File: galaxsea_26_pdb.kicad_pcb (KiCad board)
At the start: 2 copper layers, 81.5 x 54.1 mm, 18 parts, among them J1 Conn_01x10_Pin, J2 Conn_01x10_Pin, J4 Conn_01x10_Pin, U1 TPS54531DDA

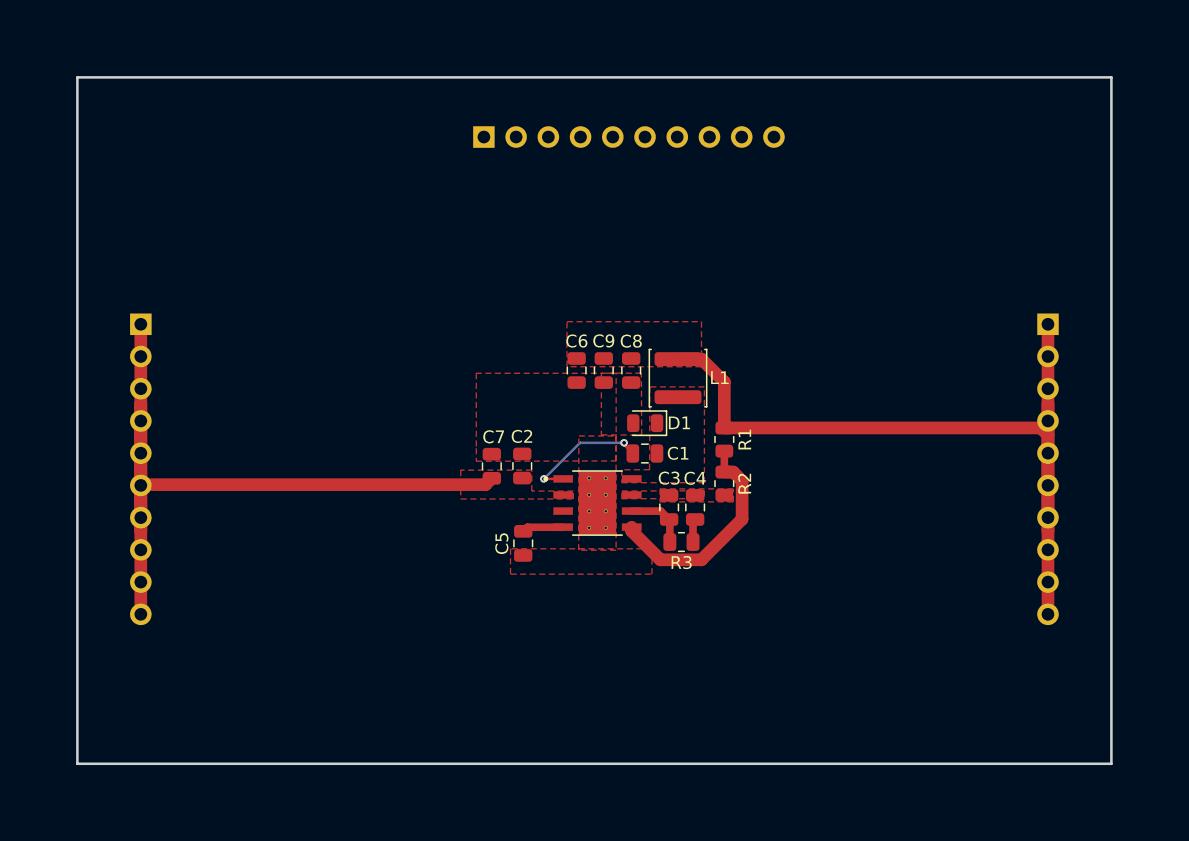
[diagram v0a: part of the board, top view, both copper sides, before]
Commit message: Add dimensions
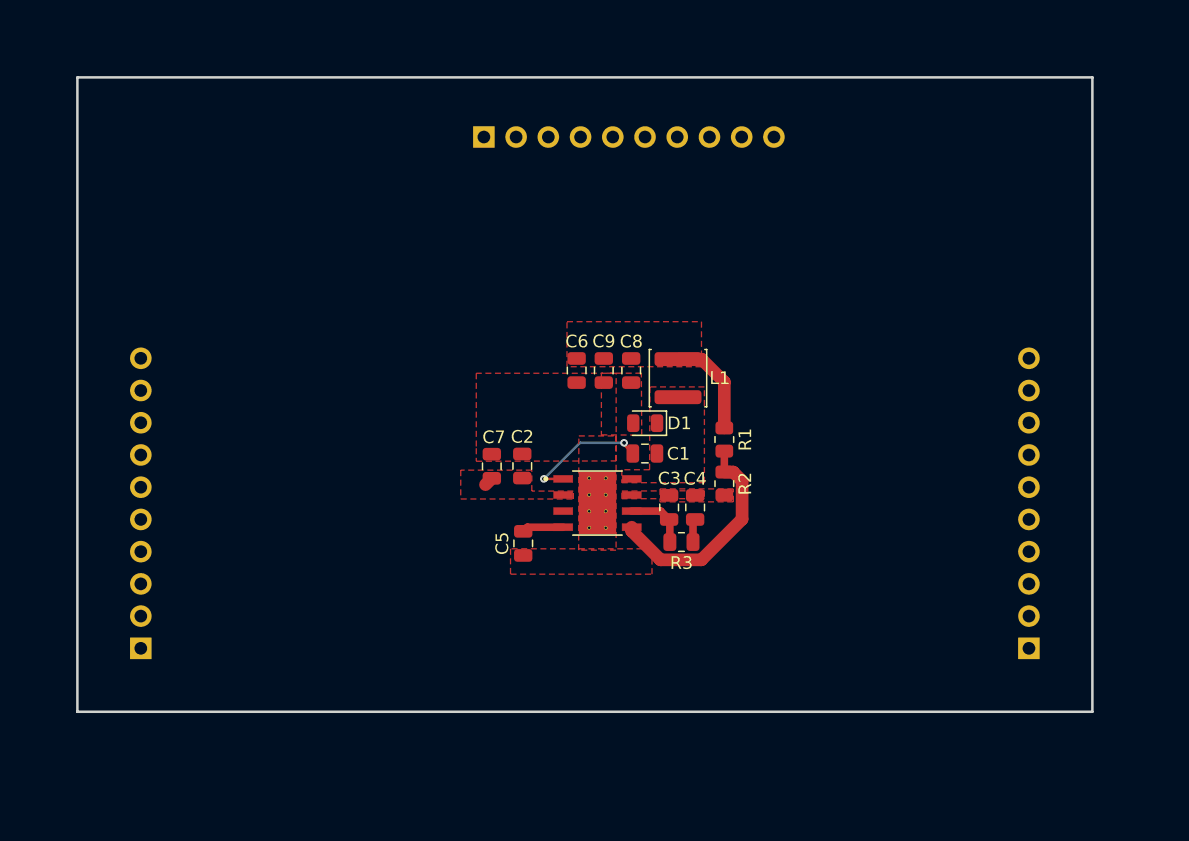
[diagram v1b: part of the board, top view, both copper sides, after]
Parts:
- moved J1 25.6 mm to (185.0, 102.8), turned to 0 degrees
- moved J2 25.5 mm to (115.0, 102.8), turned to 0 degrees
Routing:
- net /BDC_VIN: track 61.0 -> 0.74 mm
- net /BDC_VOUT: track 66.8 -> 8.02 mm
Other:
- board size 81.5 x 54.1 mm -> 80 x 50 mm

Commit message: Final pin placement
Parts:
- moved J4 27.0 mm to (115.0, 62.8)
- moved C4 0.43 mm to (158.3, 91.9)
- moved L1 0.43 mm to (156.9, 81.7)
- moved R2 0.43 mm to (160.6, 90.0)
- moved R3 0.43 mm to (157.2, 94.6)
- moved U1 0.43 mm to (150.6, 91.5)
- moved C2 0.43 mm to (144.7, 88.6)
- moved C8 0.43 mm to (153.3, 81.1)
- moved C9 0.43 mm to (151.1, 81.1)
- moved D1 0.43 mm to (154.4, 85.2)
- moved R1 0.43 mm to (160.6, 86.5)
- moved C1 0.43 mm to (154.3, 87.6)
- moved C3 0.43 mm to (156.2, 91.9)
- moved C5 0.43 mm to (144.7, 94.7)
- moved C6 0.43 mm to (149.0, 81.1)
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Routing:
- net /BDC_VIN: track 0.74 -> 51.1 mm
- net /BDC_VOUT: track 8.02 -> 55.5 mm
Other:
- board text added: "Pin 1 of each header is 5mm from corner"

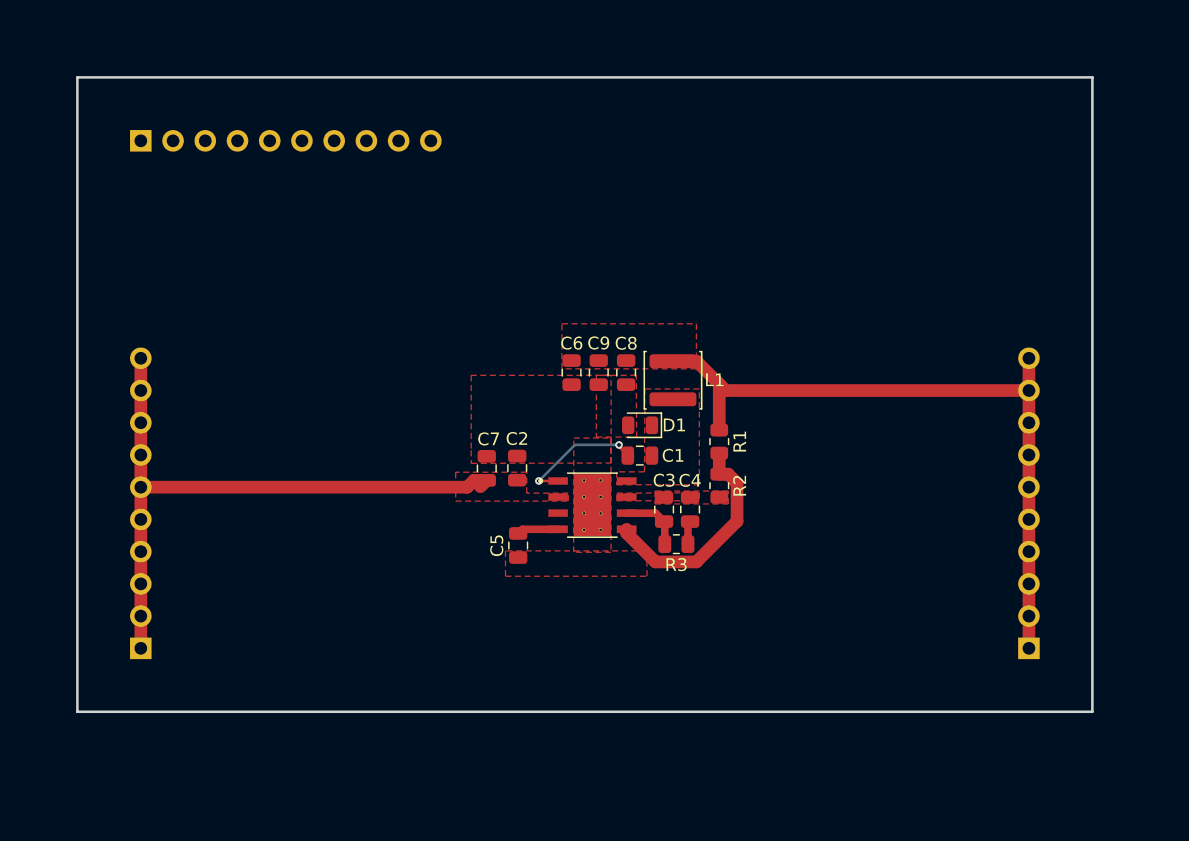
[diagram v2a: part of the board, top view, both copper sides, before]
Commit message: Organize, make BDC Module more solderable
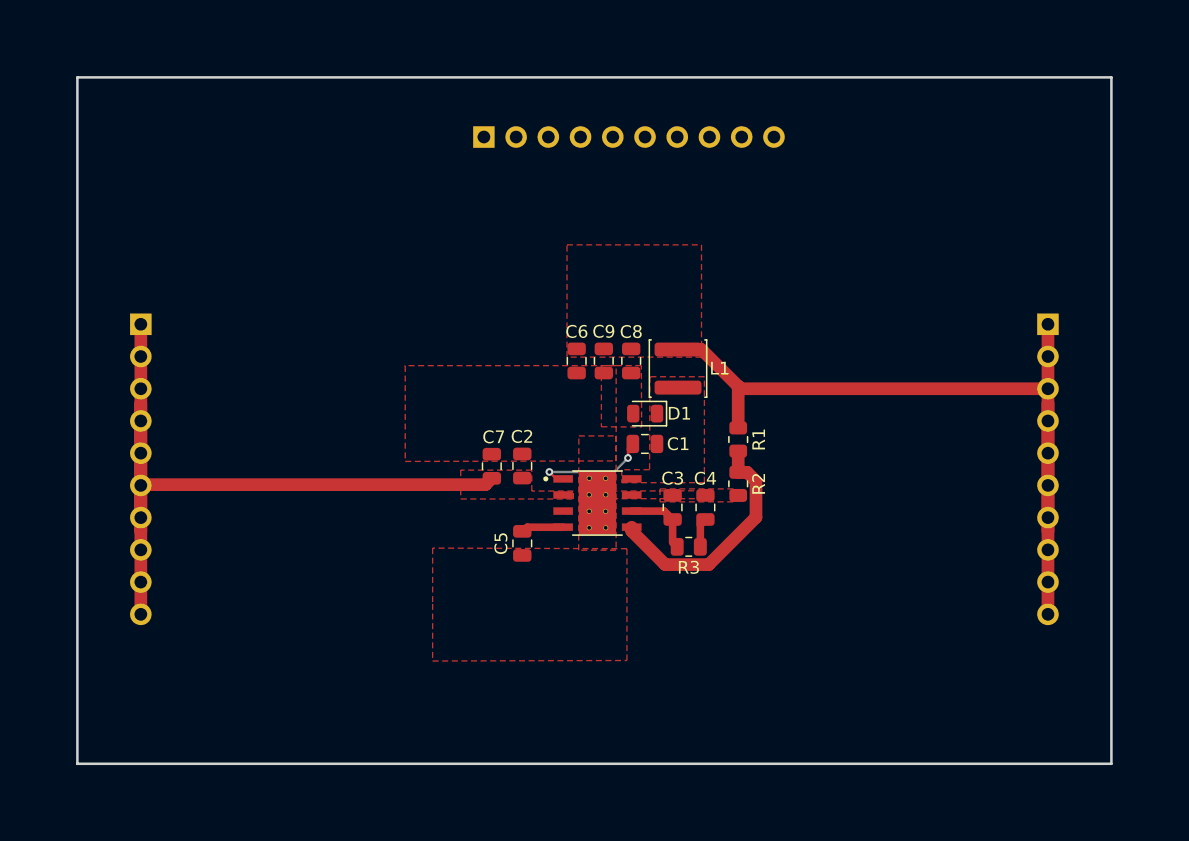
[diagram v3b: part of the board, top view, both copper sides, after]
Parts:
- moved J4 27.0 mm to (142.0, 62.5)
- moved J1 25.6 mm to (186.5, 77.3), turned to 180 degrees
- moved J2 25.5 mm to (115.0, 77.3), turned to 180 degrees
- moved R1 1.50 mm to (162.1, 86.3)
- moved R2 1.50 mm to (162.1, 89.8)
- moved C4 1.22 mm to (159.5, 91.7)
- moved D1 1.00 mm to (154.8, 84.3)
- moved L1 1.00 mm to (157.3, 80.8)
- moved C1 1.00 mm to (154.7, 86.7)
- moved C8 1.00 mm to (153.7, 80.2)
- moved C9 1.00 mm to (151.5, 80.2)
- moved C6 1.00 mm to (149.3, 80.2)
- moved R3 1.00 mm to (158.2, 94.8)
- moved C3 0.69 mm to (156.9, 91.7)
- moved U1 0.43 mm to (151.0, 91.3)
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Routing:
- net /BDC_VOUT: track 55.5 -> 66.7 mm
- net /BDC_VIN: track 51.1 -> 60.8 mm
- net /_BDC_VSENSE: track 17.6 -> 18.9 mm
- net /_BDC_BOOT: track 10.1 -> 9.24 mm
- net /_BDC_COMP: track 5.03 -> 5.80 mm
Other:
- board size 80 x 50 mm -> 81.5 x 54.1 mm
- board text removed: "Pin 1 of each header is 5mm from corner"

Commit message: Fix annotations
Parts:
- L1: value 5.6u -> 5.6u - 8.2u
- R3: renamed from R2; value 1.96k -> 1.96k - 732
- moved R1 0.56 mm to (162.1, 85.8)
- renumbered C7 to C2, C2 to C3, C3 to C4, C4 to C5, C5 to C6, C6 to C7, C9 to C8, C8 to C9, J2 to J1, J1 to J2, J4 to J3, R3 to R2
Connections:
- net /BDC_VIN renamed /BDC Module/BDC_VIN
- net /BDC_VOUT renamed /BDC Module/BDC_VOUT
- net /_BDC_BOOT renamed /BDC Module/_BDC_BOOT
- net /_BDC_COMP renamed /BDC Module/_BDC_COMP
- net /_BDC_EN renamed /BDC Module/_BDC_EN
- net /_BDC_PH renamed /BDC Module/_BDC_PH
- net /_BDC_SS renamed /BDC Module/_BDC_SS
- net /_BDC_VSENSE renamed /BDC Module/_BDC_VSENSE
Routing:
- net /BDC Module/BDC_VOUT: track 66.7 -> 66.1 mm

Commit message: pretty silkscreens
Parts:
- added TP1: VIN, TestPoint:TestPoint_Keystone_5005-5009_Compact, F.Cu at (115.0, 106.4)
- added TP2: VOUT, TestPoint:TestPoint_Keystone_5005-5009_Compact, F.Cu at (186.5, 106.4)
- added TP3: GND, TestPoint:TestPoint_Keystone_5005-5009_Compact, F.Cu at (171.2, 62.5)
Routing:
- net /BDC Module/BDC_VIN: track 60.8 -> 67.1 mm
- net /BDC Module/BDC_VOUT: track 66.1 -> 72.4 mm
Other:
- board text added: "GND"
- board text added: "VIN"
- board text added: "VOUT"

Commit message: Add GalaxSea Logo, Board Name, Author Name, Date to silkscreen
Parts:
- added G***: LOGO, LOGO, F.Cu at (127.9, 107.2)
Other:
- board text added: "TPS54531DDA Buck Converter Module Nathan Wignall ${CURRENT_DATE}"

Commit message: add Fuse, LEDs
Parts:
- added D2: LED, LED_SMD:LED_1206_3216Metric, F.Cu at (126.4, 68.7)
- added D3: LED, LED_SMD:LED_1206_3216Metric, F.Cu at (131.8, 68.7)
- added F1: Fuse_Small, Fuse:Fuse_1206_3216Metric, F.Cu at (129.6, 89.8)
- added R4: 620, Resistor_SMD:R_0603_1608Metric, F.Cu at (126.4, 73.0)
- added R5: 150/510, Resistor_SMD:R_0603_1608Metric, F.Cu at (131.8, 73.0)
- L1: value 5.6u - 8.2u -> 5.6u/8.2u
- R3: value 1.96k - 732 -> 1.96k/732
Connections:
- C2 pad 1: /BDC Module/BDC_VIN -> /BDC Module/BDC_VIN_Fuse
- C3 pad 1: /BDC Module/BDC_VIN -> /BDC Module/BDC_VIN_Fuse
- U1 pad 2: /BDC Module/BDC_VIN -> /BDC Module/BDC_VIN_Fuse
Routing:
- net /BDC Module/BDC_VIN_Fuse: track 0.00 -> 29.7 mm
- net /BDC Module/BDC_VOUT: track 72.4 -> 100.2 mm
- net /BDC Module/BDC_VIN: track 67.1 -> 52.6 mm
- net GND: track 0.00 -> 2.59 mm, vias 0 -> 2
- net Net-(D2-A): track 0.00 -> 2.12 mm
- net Net-(D3-A): track 0.00 -> 2.05 mm
- added copper zone on F.Cu, net /BDC Module/BDC_VIN_Fuse
- removed copper zone on F.Cu, net /BDC Module/BDC_VIN

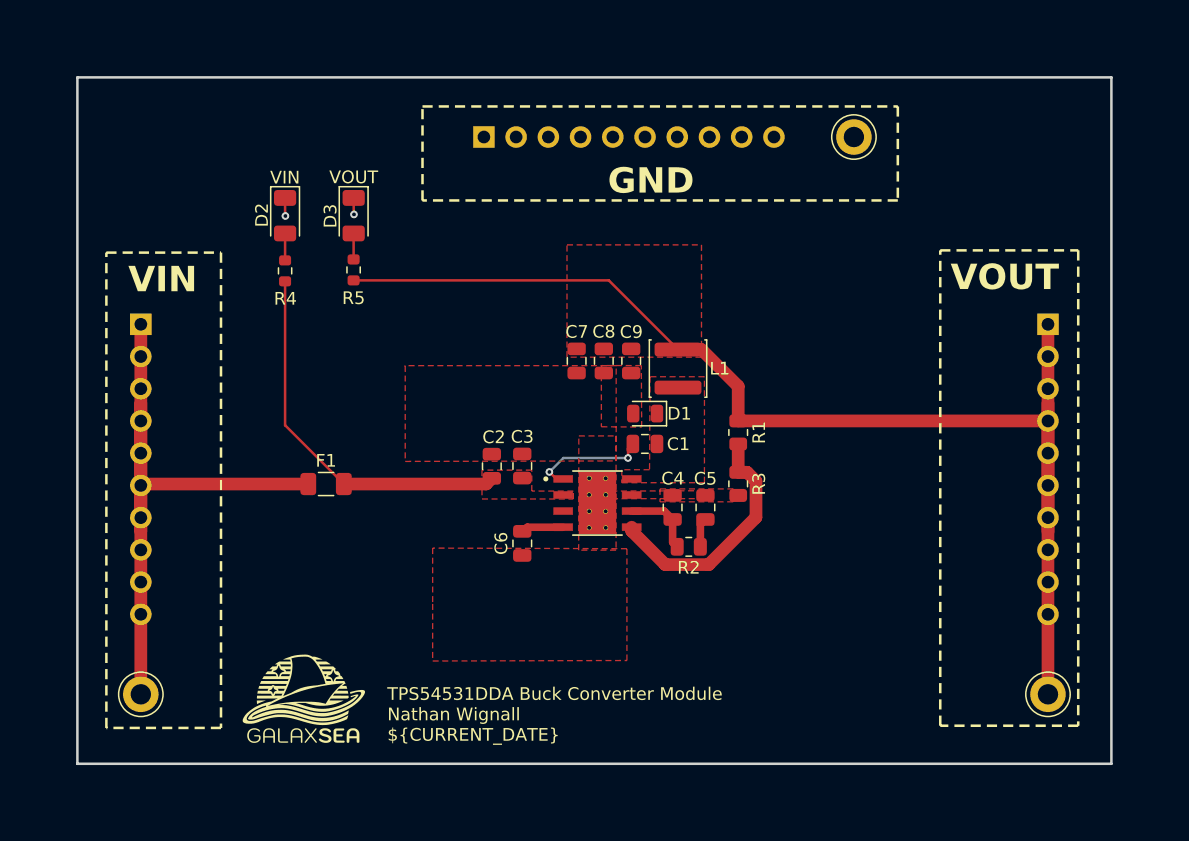
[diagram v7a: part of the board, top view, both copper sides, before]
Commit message: Round board size
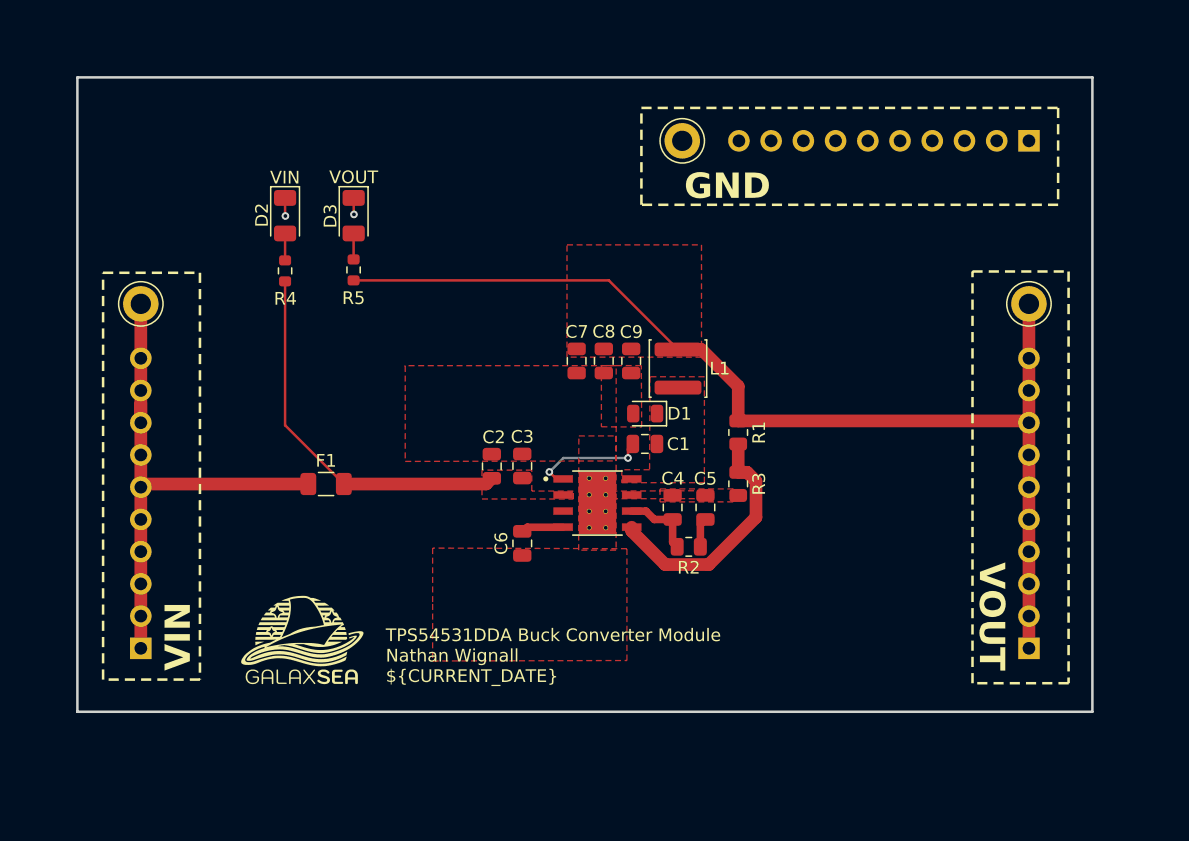
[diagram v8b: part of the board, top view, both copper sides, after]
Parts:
- moved J3 43.0 mm to (185.0, 62.8), turned to 90 degrees
- moved TP2 30.8 mm to (185.0, 75.7)
- moved TP1 30.8 mm to (115.0, 75.7)
- moved J2 25.6 mm to (185.0, 102.8), turned to 0 degrees
- moved J1 25.5 mm to (115.0, 102.8), turned to 0 degrees
- moved TP3 13.5 mm to (157.7, 62.8), turned to -90 degrees
- moved G*** 4.63 mm to (127.8, 102.5)
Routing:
- net /BDC Module/BDC_VOUT: track 100.2 -> 86.6 mm
- net /BDC Module/BDC_VIN: track 52.6 -> 41.8 mm
- net /BDC Module/_BDC_BOOT: track 9.24 -> 8.16 mm
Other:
- board size 81.5 x 54.1 mm -> 80 x 50 mm
